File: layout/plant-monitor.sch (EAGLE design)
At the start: 11 parts, among them J1 AVR_SPI_PRG_6PTH

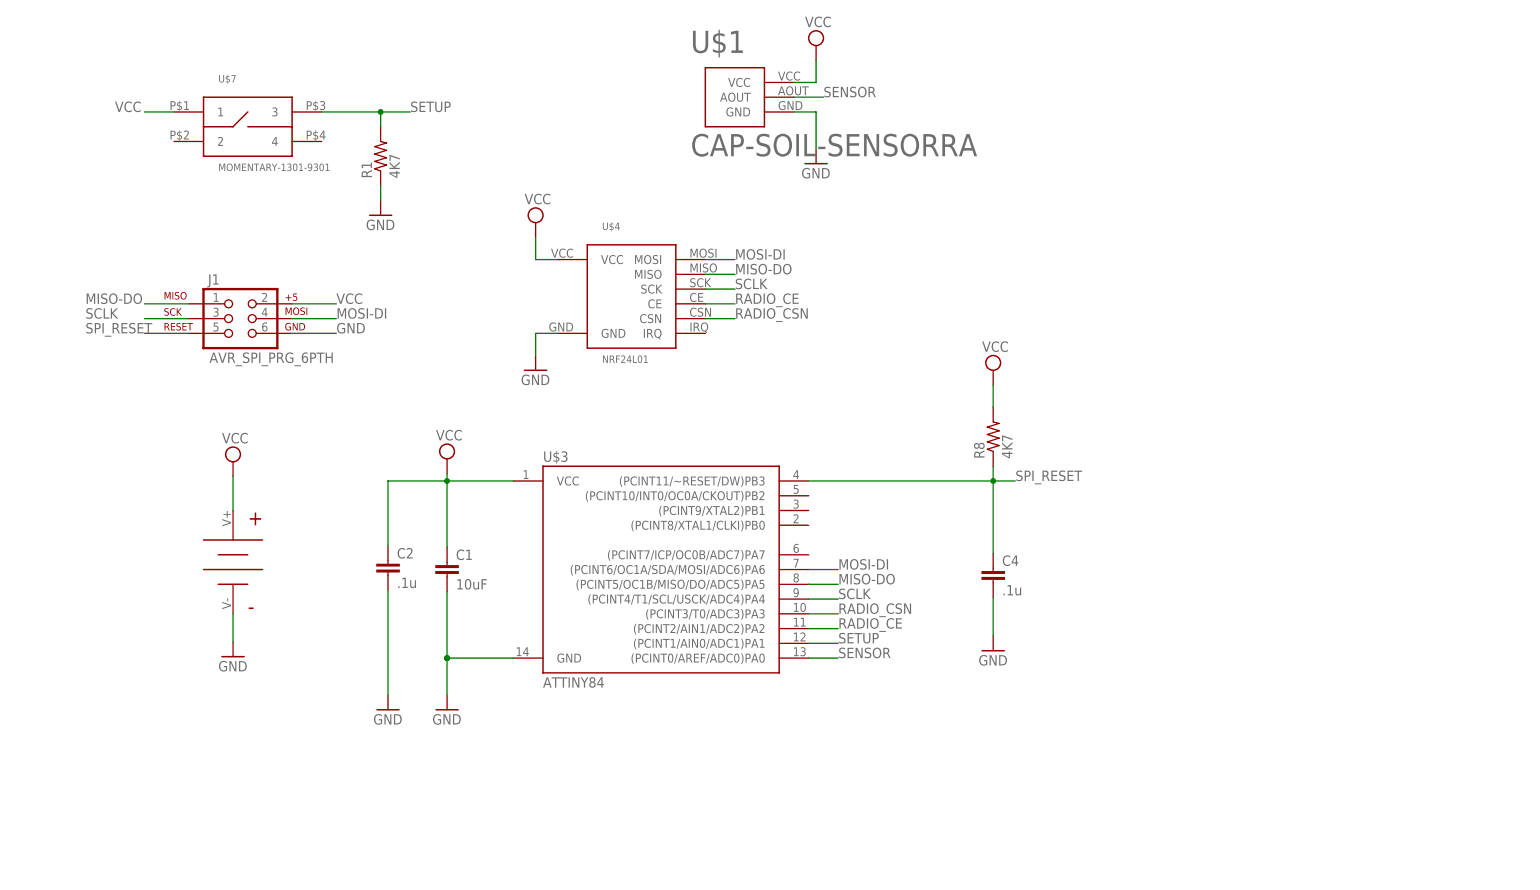
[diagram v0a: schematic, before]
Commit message: Updated design to address problems in v1.3 board, notably ower switching added for soil sensor
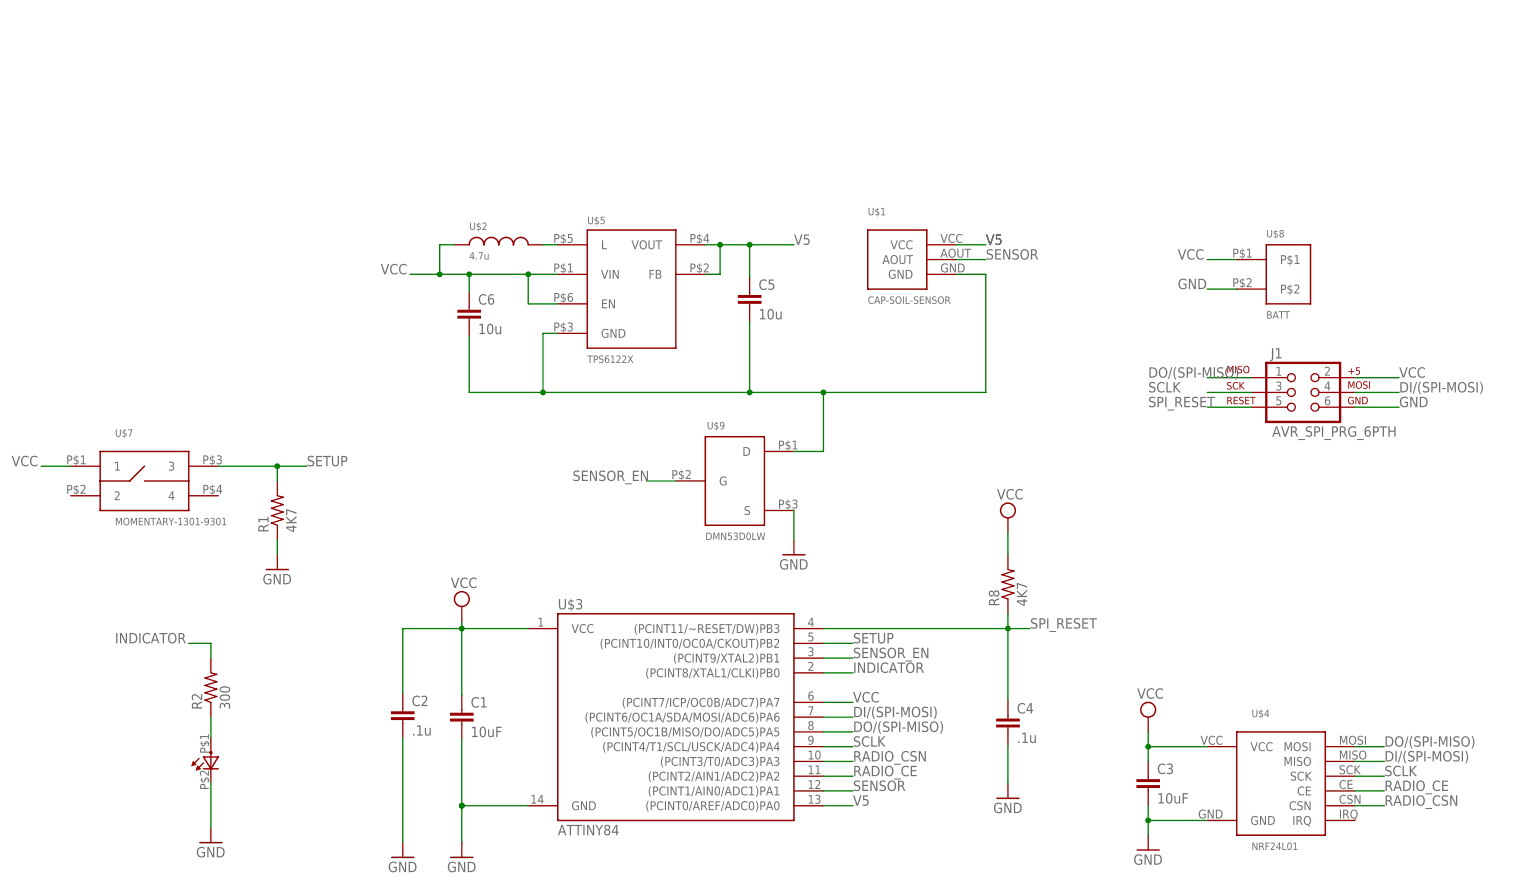
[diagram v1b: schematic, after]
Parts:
- added C3: 10uF, SparkFun-Capacitors:10UF-1206-6.3V-20%
- added C5, C6: 10u, SparkFun:CAP0805
- added R2: 300, SparkFun:RESISTOR
- added U$5: TPS6122X, GARTH:TPS6122X
- added U$6: LED, GARTH:LED
- added U$8: BATT, GARTH:JST-PH-2
- added U$9: DMN53D0LW, GARTH:DMN53D0LW
- U$1: value CAP-SOIL-SENSORRA -> CAP-SOIL-SENSOR; device GARTH:CAP-SOIL-SENSORRA -> GARTH:CAP-SOIL-SENSOR
- U$2: value 20MM-COIN-BATT -> 4.7u; device GARTH:20MM-COIN-BATT -> GARTH:INDUCTORLQH3NPN
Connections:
- removed net MISO-DO: J1.1, U$3.(PCINT5/OC1B/MISO/DO/ADC5)PA5, U$4.MISO
- removed net MOSI-DI: J1.4, U$3.(PCINT6/OC1A/SDA/MOSI/ADC6)PA6, U$4.MOSI
- new net DI/(SPI-MOSI): J1.4, U$3.(PCINT6/OC1A/SDA/MOSI/ADC6)PA6, U$4.MISO
- new net DO/(SPI-MISO): J1.1, U$3.(PCINT5/OC1B/MISO/DO/ADC5)PA5, U$4.MOSI
- new net INDICATOR: R2.2, U$3.(PCINT8/XTAL1/CLKI)PB0
- new net N$1: R2.1, U$6.A
- new net N$2: U$2.2, U$5.L
- new net N$5: C5.2, C6.2, U$1.GND, U$5.GND, U$9.D
- new net SENSOR_EN: U$3.(PCINT9/XTAL2)PB1, U$9.G
- new net V5: C5.1, U$1.VCC, U$3.(PCINT0/AREF/ADC0)PA0, U$5.FB, U$5.VOUT
- net GND: now also C3.2, U$6.C, U$8.P$2, U$9.S; no longer U$1.GND, U$2.V-
- net SENSOR: now also U$3.(PCINT1/AIN0/ADC1)PA1; no longer U$3.(PCINT0/AREF/ADC0)PA0
- net SETUP: now also U$3.(PCINT10/INT0/OC0A/CKOUT)PB2; no longer U$3.(PCINT1/AIN0/ADC1)PA1
- net VCC: now also C3.1, C6.1, U$2.1, U$3.(PCINT7/ICP/OC0B/ADC7)PA7, U$5.EN, U$5.VIN, U$8.P$1; no longer U$1.VCC, U$2.V+
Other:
- moved on the sheet: C1, C2, C4, J1, R1, R8, U$1, U$3, U$4, U$7

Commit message: Updated board design that removes the voltage regulator.  The moisture meter does this and its not necessary
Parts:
- removed C5, C6: 10u, SparkFun:CAP0805
- removed U$2: 4.7u, GARTH:INDUCTORLQH3NPN
- removed U$5: TPS6122X, GARTH:TPS6122X
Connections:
- removed net N$2: U$2.2, U$5.L
- removed net V5: C5.1, U$1.VCC, U$3.(PCINT0/AREF/ADC0)PA0, U$5.FB, U$5.VOUT
- net N$5: no longer C5.2, C6.2, U$5.GND
- net VCC: now also U$1.VCC; no longer C6.1, U$2.1, U$5.EN, U$5.VIN
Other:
- moved on the sheet: U$1
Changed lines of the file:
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@@
 <?xml version="1.0" encoding="utf-8"?>
 <!DOCTYPE eagle SYSTEM "eagle.dtd">
-<eagle version="9.5.2">
+<eagle version="9.6.1">
 <drawing>
 <settings>
@@
 <part name="GND5" library="supply1" library_urn="urn:adsk.eagle:library:371" deviceset="GND" device=""/>
 <part name="GND6" library="supply1" library_urn="urn:adsk.eagle:library:371" deviceset="GND" device=""/>
-<part name="C5" library="SparkFun" deviceset="CAP" device="0805" value="10u"/>
-<part name="C6" library="SparkFun" deviceset="CAP" device="0805" value="10u"/>
-<part name="U$5" library="GARTH" deviceset="TPS6122X" device=""/>
 <part name="U$8" library="GARTH" deviceset="JST-PH-2" device="" value="BATT"/>
-<part name="U$2" library="GARTH" deviceset="INDUCTOR" device="LQH3NPN" value="4.7u"/>
 <part name="U$6" library="GARTH" deviceset="LED" device=""/>
 <part name="R2" library="SparkFun" deviceset="RESISTOR" device="" value="300"/>
@@
 <attribute name="VALUE" x="26.67" y="-3.81" size="1.778" layer="96"/>
 </instance>
-<instance part="U$1" gate="G$1" x="104.14" y="101.6" smashed="yes">
-<attribute name="NAME" x="99.06" y="109.22" size="1.27" layer="95"/>
-<attribute name="VALUE" x="99.06" y="93.98" size="1.27" layer="96"/>
+<instance part="U$1" gate="G$1" x="76.2" y="88.9" smashed="yes">
+<attribute name="NAME" x="71.12" y="96.52" size="1.27" layer="95"/>
+<attribute name="VALUE" x="71.12" y="81.28" size="1.27" layer="96"/>
 </instance>
 <instance part="U$4" gate="G$1" x="170.18" y="12.7" smashed="yes">
@@
 <attribute name="VALUE" x="16.51" y="-3.81" size="1.778" layer="96"/>
 </instance>
-<instance part="C5" gate="G$1" x="78.74" y="93.472" smashed="yes">
-<attribute name="NAME" x="80.264" y="96.393" size="1.778" layer="95"/>
-<attribute name="VALUE" x="80.264" y="91.313" size="1.778" layer="96"/>
-</instance>
-<instance part="C6" gate="G$1" x="30.48" y="90.932" smashed="yes">
-<attribute name="NAME" x="32.004" y="93.853" size="1.778" layer="95"/>
-<attribute name="VALUE" x="32.004" y="88.773" size="1.778" layer="96"/>
-</instance>
-<instance part="U$5" gate="G$1" x="58.42" y="96.52" smashed="yes">
-<attribute name="NAME" x="50.8" y="107.696" size="1.27" layer="95"/>
-<attribute name="VALUE" x="50.8" y="83.82" size="1.27" layer="96"/>
-</instance>
 <instance part="U$8" gate="G$1" x="170.18" y="99.06" smashed="yes">
 <attribute name="NAME" x="167.64" y="105.41" size="1.27" layer="95"/>
 <attribute name="VALUE" x="167.64" y="91.44" size="1.27" layer="96"/>
-</instance>
-<instance part="U$2" gate="G$1" x="35.56" y="104.14" smashed="yes">
-<attribute name="NAME" x="30.48" y="106.68" size="1.27" layer="95"/>
-<attribute name="VALUE" x="30.48" y="101.6" size="1.27" layer="96"/>
 </instance>
 <instance part="U$6" gate="G$1" x="-13.97" y="14.224" smashed="yes"/>
@@
 </segment>
 <segment>
-<pinref part="U$5" gate="G$1" pin="VIN"/>
-<wire x1="45.72" y1="99.06" x2="40.64" y2="99.06" width="0.1524" layer="91"/>
-<wire x1="40.64" y1="99.06" x2="30.48" y2="99.06" width="0.1524" layer="91"/>
-<wire x1="30.48" y1="99.06" x2="25.4" y2="99.06" width="0.1524" layer="91"/>
-<wire x1="25.4" y1="99.06" x2="20.32" y2="99.06" width="0.1524" layer="91"/>
-<wire x1="27.94" y1="104.14" x2="25.4" y2="104.14" width="0.1524" layer="91"/>
-<wire x1="25.4" y1="104.14" x2="25.4" y2="99.06" width="0.1524" layer="91"/>
-<junction x="25.4" y="99.06"/>
-<pinref part="U$5" gate="G$1" pin="EN"/>
-<wire x1="45.72" y1="93.98" x2="40.64" y2="93.98" width="0.1524" layer="91"/>
-<wire x1="40.64" y1="93.98" x2="40.64" y2="99.06" width="0.1524" layer="91"/>
-<junction x="40.64" y="99.06"/>
-<pinref part="C6" gate="G$1" pin="1"/>
-<wire x1="30.48" y1="96.012" x2="30.48" y2="99.06" width="0.1524" layer="91"/>
-<junction x="30.48" y="99.06"/>
-<label x="15.24" y="99.06" size="1.778" layer="95"/>
-<pinref part="U$2" gate="G$1" pin="1"/>
-</segment>
-<segment>
 <pinref part="U$4" gate="G$1" pin="VCC"/>
 <wire x1="157.48" y1="17.78" x2="147.32" y2="17.78" width="0.1524" layer="91"/>
@@
 <wire x1="147.32" y1="15.24" x2="147.32" y2="17.78" width="0.1524" layer="91"/>
 <junction x="147.32" y="17.78"/>
+</segment>
+<segment>
+<pinref part="U$1" gate="G$1" pin="VCC"/>
+<wire x1="86.36" y1="91.44" x2="93.98" y2="91.44" width="0.1524" layer="91"/>
+<label x="96.52" y="91.44" size="1.778" layer="95"/>
 </segment>
 </net>
@@
 <segment>
 <pinref part="U$1" gate="G$1" pin="AOUT"/>
-<wire x1="114.3" y1="101.6" x2="119.38" y2="101.6" width="0.1524" layer="91"/>
-<label x="119.38" y="101.6" size="1.778" layer="95"/>
+<wire x1="86.36" y1="88.9" x2="93.98" y2="88.9" width="0.1524" layer="91"/>
+<label x="96.52" y="88.9" size="1.778" layer="95"/>
 </segment>
 <segment>
@@
 </segment>
 </net>
-<net name="N$2" class="0">
-<segment>
-<pinref part="U$5" gate="G$1" pin="L"/>
-<wire x1="45.72" y1="104.14" x2="43.18" y2="104.14" width="0.1524" layer="91"/>
-<pinref part="U$2" gate="G$1" pin="2"/>
-</segment>
-</net>
-<net name="V5" class="0">
-<segment>
-<pinref part="U$5" gate="G$1" pin="VOUT"/>
-<wire x1="71.12" y1="104.14" x2="73.66" y2="104.14" width="0.1524" layer="91"/>
-<pinref part="U$5" gate="G$1" pin="FB"/>
-<wire x1="73.66" y1="104.14" x2="78.74" y2="104.14" width="0.1524" layer="91"/>
-<wire x1="78.74" y1="104.14" x2="86.36" y2="104.14" width="0.1524" layer="91"/>
-<wire x1="71.12" y1="99.06" x2="73.66" y2="99.06" width="0.1524" layer="91"/>
-<wire x1="73.66" y1="99.06" x2="73.66" y2="104.14" width="0.1524" layer="91"/>
-<junction x="73.66" y="104.14"/>
-<pinref part="C5" gate="G$1" pin="1"/>
-<wire x1="78.74" y1="98.552" x2="78.74" y2="104.14" width="0.1524" layer="91"/>
-<junction x="78.74" y="104.14"/>
-<label x="86.36" y="104.14" size="1.778" layer="95"/>
-</segment>
-<segment>
-<pinref part="U$1" gate="G$1" pin="VCC"/>
-<wire x1="114.3" y1="104.14" x2="119.38" y2="104.14" width="0.1524" layer="91"/>
-<label x="119.38" y="104.14" size="1.778" layer="95"/>
-<label x="119.38" y="104.14" size="1.778" layer="95"/>
-</segment>
-<segment>
-<pinref part="U$3" gate="G$1" pin="(PCINT0/AREF/ADC0)PA0"/>
-<wire x1="91.44" y1="7.62" x2="96.52" y2="7.62" width="0.1524" layer="91"/>
-<label x="96.52" y="7.62" size="1.778" layer="95"/>
-</segment>
-</net>
 <net name="N$1" class="0">
 <segment>
@@
 <net name="N$5" class="0">
 <segment>
-<pinref part="C5" gate="G$1" pin="2"/>
-<wire x1="78.74" y1="90.932" x2="78.74" y2="78.74" width="0.1524" layer="91"/>
-<pinref part="U$5" gate="G$1" pin="GND"/>
-<wire x1="45.72" y1="88.9" x2="43.18" y2="88.9" width="0.1524" layer="91"/>
-<pinref part="C6" gate="G$1" pin="2"/>
-<wire x1="30.48" y1="88.392" x2="30.48" y2="78.74" width="0.1524" layer="91"/>
-<wire x1="30.48" y1="78.74" x2="43.18" y2="78.74" width="0.1524" layer="91"/>
-<wire x1="43.18" y1="78.74" x2="78.74" y2="78.74" width="0.1524" layer="91"/>
-<wire x1="78.74" y1="78.74" x2="91.44" y2="78.74" width="0.1524" layer="91"/>
-<wire x1="91.44" y1="78.74" x2="91.44" y2="68.58" width="0.1524" layer="91"/>
+<wire x1="91.44" y1="86.36" x2="91.44" y2="68.58" width="0.1524" layer="91"/>
 <pinref part="U$9" gate="G$1" pin="D"/>
 <wire x1="91.44" y1="68.58" x2="86.36" y2="68.58" width="0.1524" layer="91"/>
 <pinref part="U$1" gate="G$1" pin="GND"/>
-<wire x1="114.3" y1="99.06" x2="119.38" y2="99.06" width="0.1524" layer="91"/>
-<wire x1="119.38" y1="99.06" x2="119.38" y2="78.74" width="0.1524" layer="91"/>
-<wire x1="119.38" y1="78.74" x2="91.44" y2="78.74" width="0.1524" layer="91"/>
-<junction x="91.44" y="78.74"/>
-<wire x1="43.18" y1="88.9" x2="43.18" y2="78.74" width="0.1524" layer="91"/>
-<junction x="43.18" y="78.74"/>
-<junction x="78.74" y="78.74"/>
-</segment>
-</net>
+<wire x1="86.36" y1="86.36" x2="91.44" y2="86.36" width="0.1524" layer="91"/>
+</segment>
+</net>
